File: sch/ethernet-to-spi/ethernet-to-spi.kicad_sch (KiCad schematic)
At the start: 28 parts, among them J1 G8X-188S7-BP, J2 mosi, J3 sck_tx, J4 mosi_tx, J5 cs, J6 sck, J7 vcc, J8 gnd, Q1 Q_NMOS_DGS, Q2 Q_NMOS_DGS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

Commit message: Fix first edge filter circuit, create PCB
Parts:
- removed Q1, Q2: Q_NMOS_DGS, symbol Device:Q_NMOS_DGS
- added C10: 10p, Capacitor_SMD:C_0805_2012Metric, symbol Device:C
- added Q1, Q2: 2N7002, Package_TO_SOT_SMD:SOT-23, symbol Device:Q_NMOS_GSD
- added R5: 1k, Resistor_THT:R_Axial_DIN0207_L6.3mm_D2.5mm_P15.24mm_Horizontal, symbol Device:R
- added TP1, TP2, TP3, TP4: TestPoint, TestPoint:TestPoint_Pad_D3.0mm, symbol Connector:TestPoint
- C1, C2, C3, C4, C5, C6, C7, C8, C9: footprint (none) -> Capacitor_SMD:C_0805_2012Metric
- J2, J3, J4, J5, J6, J7, J8: footprint (none) -> Connector_Wire:SolderWire-0.25sqmm_1x01_D0.65mm_OD2mm_Relief
- R1, R2, R3: footprint (none) -> Resistor_SMD:R_0805_2012Metric
- R4: value 1k -> 500; footprint (none) -> Resistor_SMD:R_0805_2012Metric
- U1: renamed from U2; footprint (none) -> Package_SO:SOIC-14_3.9x8.7mm_P1.27mm
- U2: renamed from U3; footprint (none) -> Package_SO:SOIC-14_3.9x8.7mm_P1.27mm
- U3: renamed from U4; footprint (none) -> Package_DIP:DIP-16_W7.62mm
- U4: renamed from U1; footprint (none) -> Package_SO:SOIC-14_3.9x8.7mm_P1.27mm
- U5: footprint (none) -> Package_SO:SOIC-14_3.9x8.7mm_P1.27mm
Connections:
- net GND: now also U2.1, U4.1, U4.2, U5.1, U5.2, C10.2, Q1.2 (S), Q2.2 (S); no longer U1.2, U1.5, U5.4, U5.5
- net VCC: now also U1.13, U1.9, U5.10, U5.9; no longer U2.13, U4.12, U4.13, U5.12, U5.13
- net edge: now also U4.10, U4.11, TP4.1; no longer U4.3, U4.4
- net edge_in: now also U1.6, U4.13, Q1.1 (G), TP2.1; no longer U1.8, U4.1
- net line: now also U1.12, U1.4; no longer U1.1, U1.9
- net line_delayed: now also U1.5, U1.8; no longer U1.10, U1.6
- net sck: now also U2.10, U2.9; no longer U2.4, U2.5
- net ~{idle}: now also U2.12, U5.12; no longer U2.2, U5.1
- net ~{line}: now also U1.10, U1.11, R5.1; no longer U1.3, U1.4, U5.2
- net at J4.1 (Pin_1): now also U1.2; no longer U1.12
- net at J3.1 (Pin_1): now also U1.1; no longer U1.13
- net at U2.6: no longer U4.5
- net at U2.8: now also U4.9
- net at U2.11: now also C9.2, R4.2, Q2.3 (D), TP3.1; no longer U2.12
- net at C8.2, R3.2: now also U2.13, Q1.3 (D); no longer U2.1
- net at U3.15 (1D): now also U1.3; no longer U1.11
- net at U5.3: now also U5.4, U5.5; no longer U4.2
- net at U4.8: now also Q2.1 (G), TP1.1
- new net: U4.12, U5.11
- new net: C10.1, R5.2, U5.13
- new net: U2.4, U2.5
- new net: U2.2, U2.3
- new net: U4.3, U4.4, U4.5
- no-connect marks 11 -> 12
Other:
- moved on the sheet: U1A, U1B, U1C, U1D, U2A, U2B, U2C, U2D, U2E, U2F, U4A, U4B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

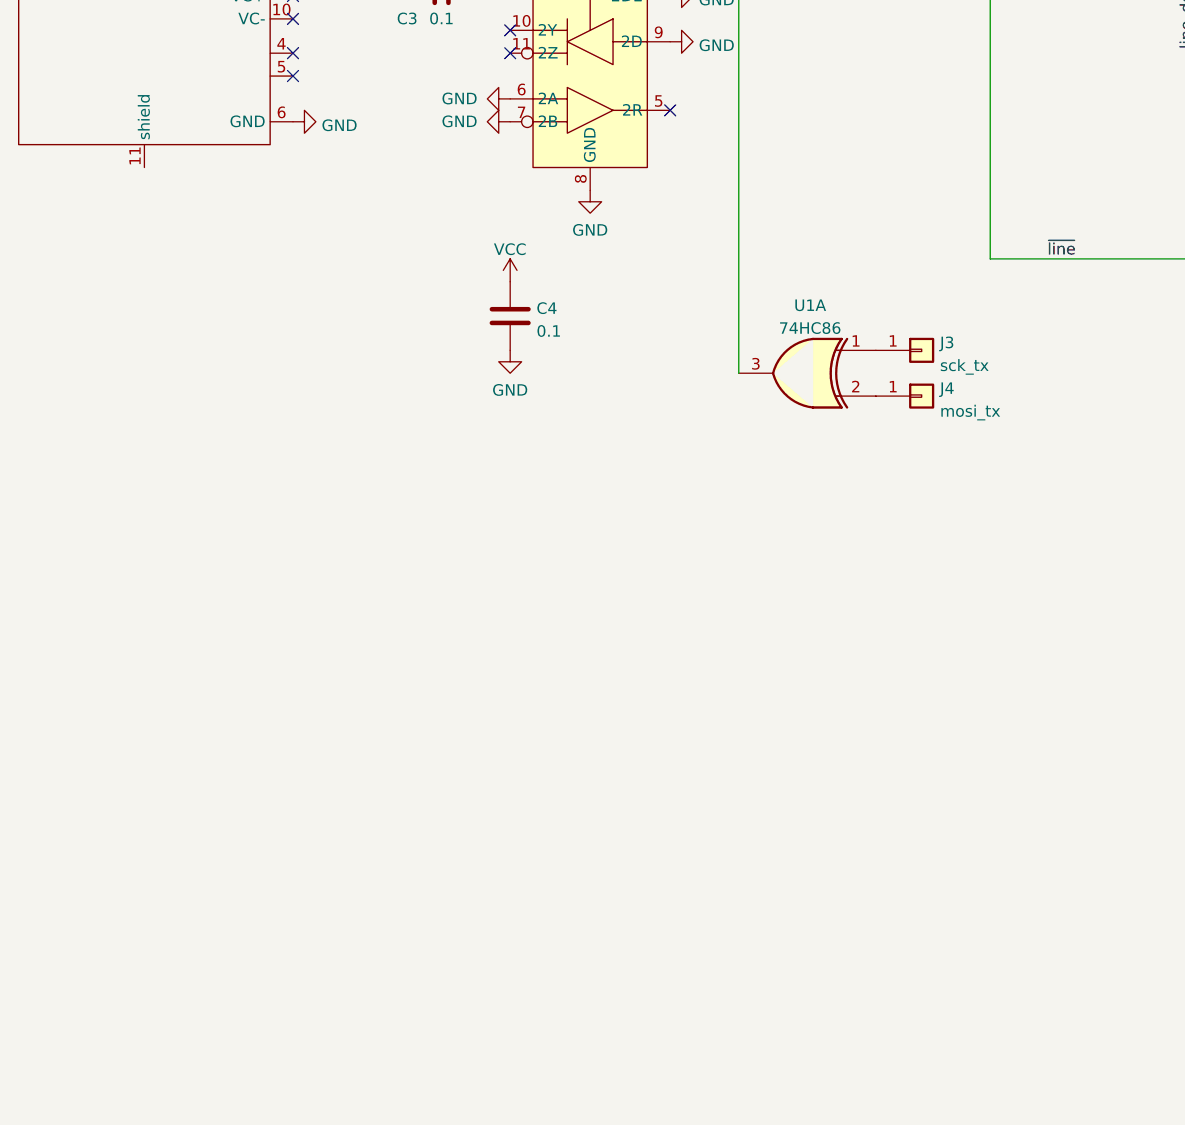
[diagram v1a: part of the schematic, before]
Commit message: Add level shifters for inputs
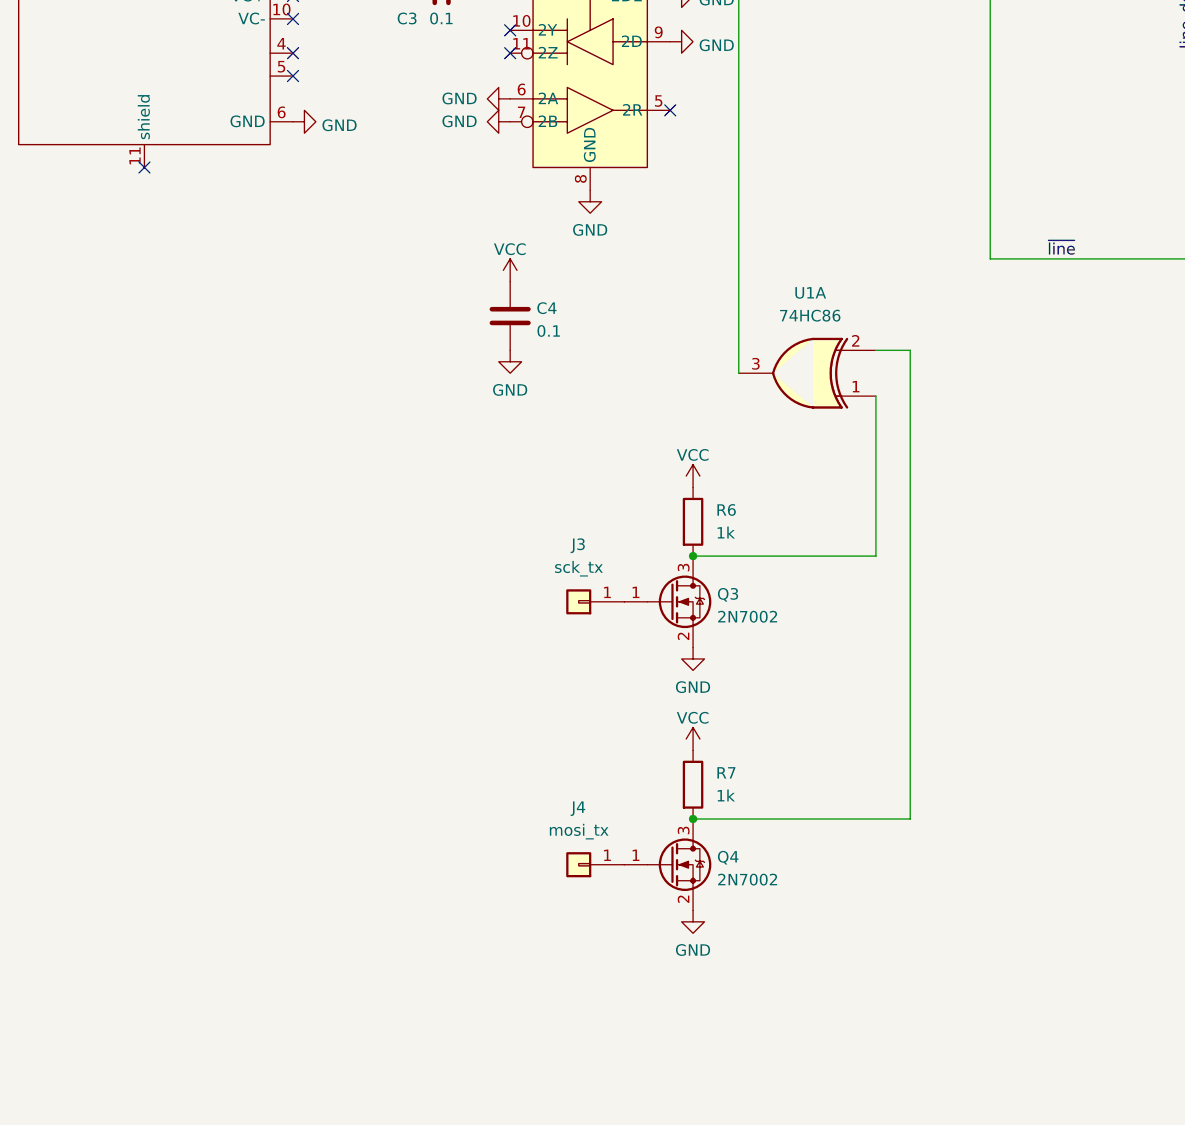
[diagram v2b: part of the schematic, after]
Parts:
- added Q3, Q4: 2N7002, Package_TO_SOT_SMD:SOT-23, symbol Device:Q_NMOS_GSD
- added R6, R7: 1k, Resistor_SMD:R_0805_2012Metric, symbol Device:R
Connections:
- net GND: now also Q3.2 (S), Q4.2 (S)
- net VCC: now also R6.1, R7.1
- net at J4.1 (Pin_1): now also Q4.1 (G); no longer U1.2
- net at J3.1 (Pin_1): now also Q3.1 (G); no longer U1.1
- new net: Q4.3 (D), R7.2, U1.2
- new net: Q3.3 (D), R6.2, U1.1
- no-connect marks 12 -> 13
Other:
- moved on the sheet: J3, J4, U1A

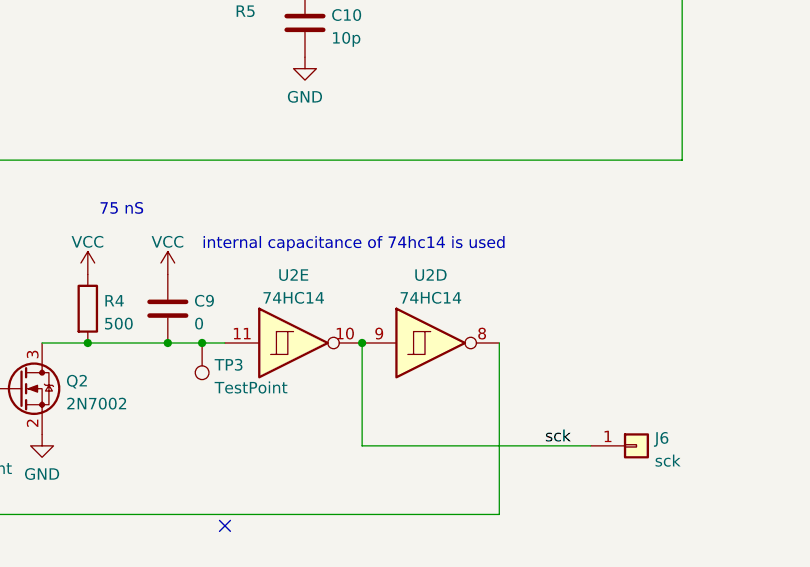
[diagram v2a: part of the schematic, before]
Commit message: Update capacitor value for 75 nS delay
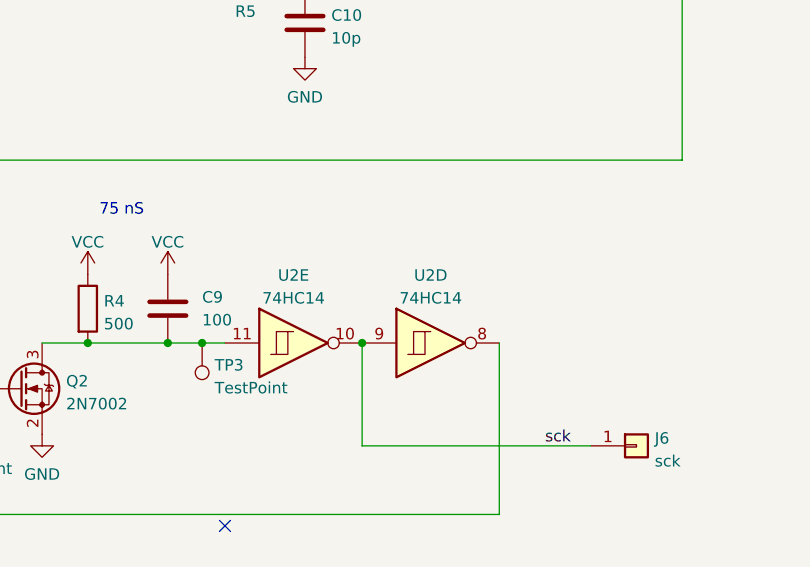
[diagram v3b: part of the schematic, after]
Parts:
- C9: value 0 -> 100
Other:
- note removed: "internal capacitance of 74hc14 is used"
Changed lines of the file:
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@@
-    (effects (font (size 1.27 1.27)) (justify left bottom))
-  )
-  (text "internal capacitance of 74hc14 is used" (at 208.28 110.49 0)
     (effects (font (size 1.27 1.27)) (justify left bottom))
   )
@@
   (symbol (lib_id "Device:C") (at 204.47 116.84 0) (unit 1)
     (in_bom yes) (on_board yes) (fields_autoplaced)
-    (property "Reference" "C9" (id 0) (at 207.391 116.0053 0)
-      (effects (font (size 1.27 1.27)) (justify left))
-    )
-    (property "Value" "0" (id 1) (at 207.391 118.5422 0)
+    (property "Reference" "C9" (id 0) (at 208.28 115.5699 0)
+      (effects (font (size 1.27 1.27)) (justify left))
+    )
+    (property "Value" "100" (id 1) (at 208.28 118.1099 0)
       (effects (font (size 1.27 1.27)) (justify left))
     )
@@
     )
     (path "/7da41d05-d663-430f-a917-43d4b56a6830"
-      (reference "C9") (unit 1) (value "0") (footprint "Capacitor_SMD:C_0805_2012Metric")
+      (reference "C9") (unit 1) (value "100") (footprint "Capacitor_SMD:C_0805_2012Metric")
     )
     (path "/251ebc69-a977-4dd5-8ba7-0315bea79bbb"
